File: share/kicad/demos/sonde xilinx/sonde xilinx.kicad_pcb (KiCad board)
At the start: 2 copper layers, 81.3 x 43.2 mm, 25 parts, among them J1 DB25MALE, J2 DB9MALE, P1 CONN_6, U1 74LS125, U2 74LS125

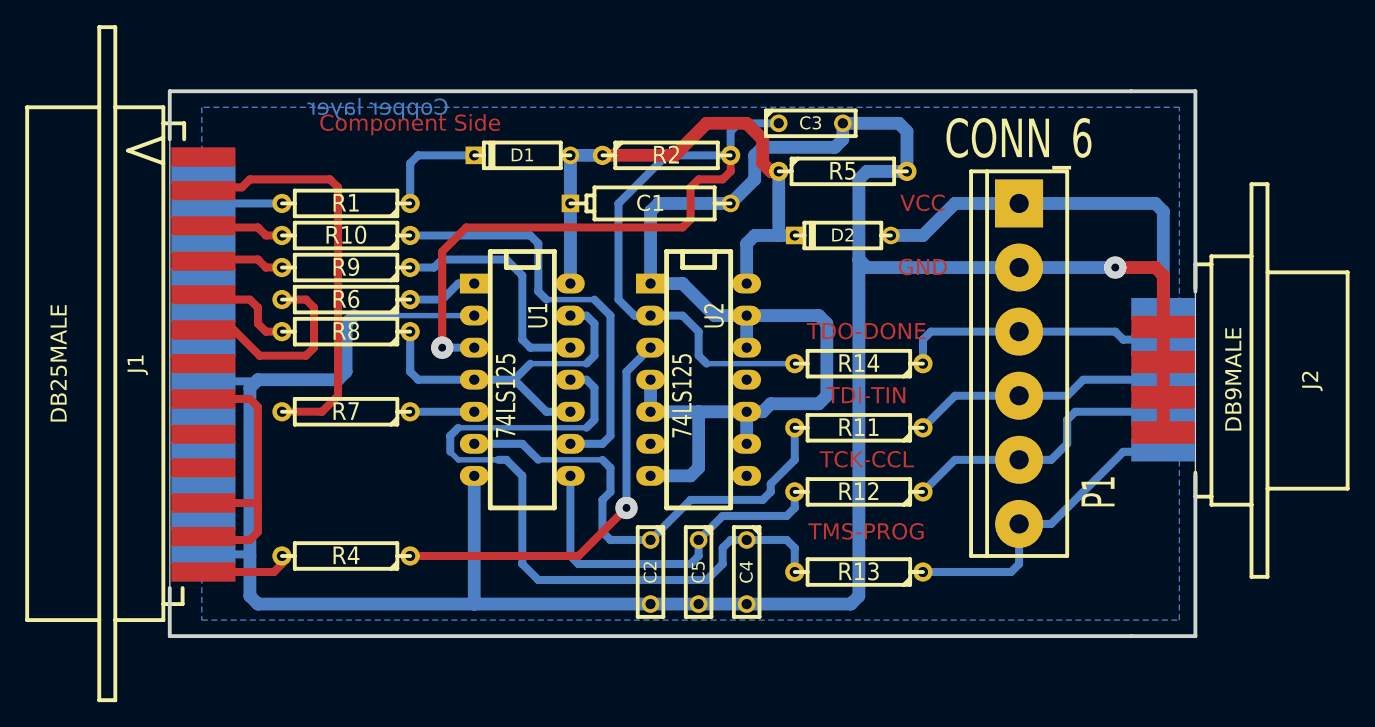
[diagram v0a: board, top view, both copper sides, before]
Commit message: Remove KiCad V4.0.7
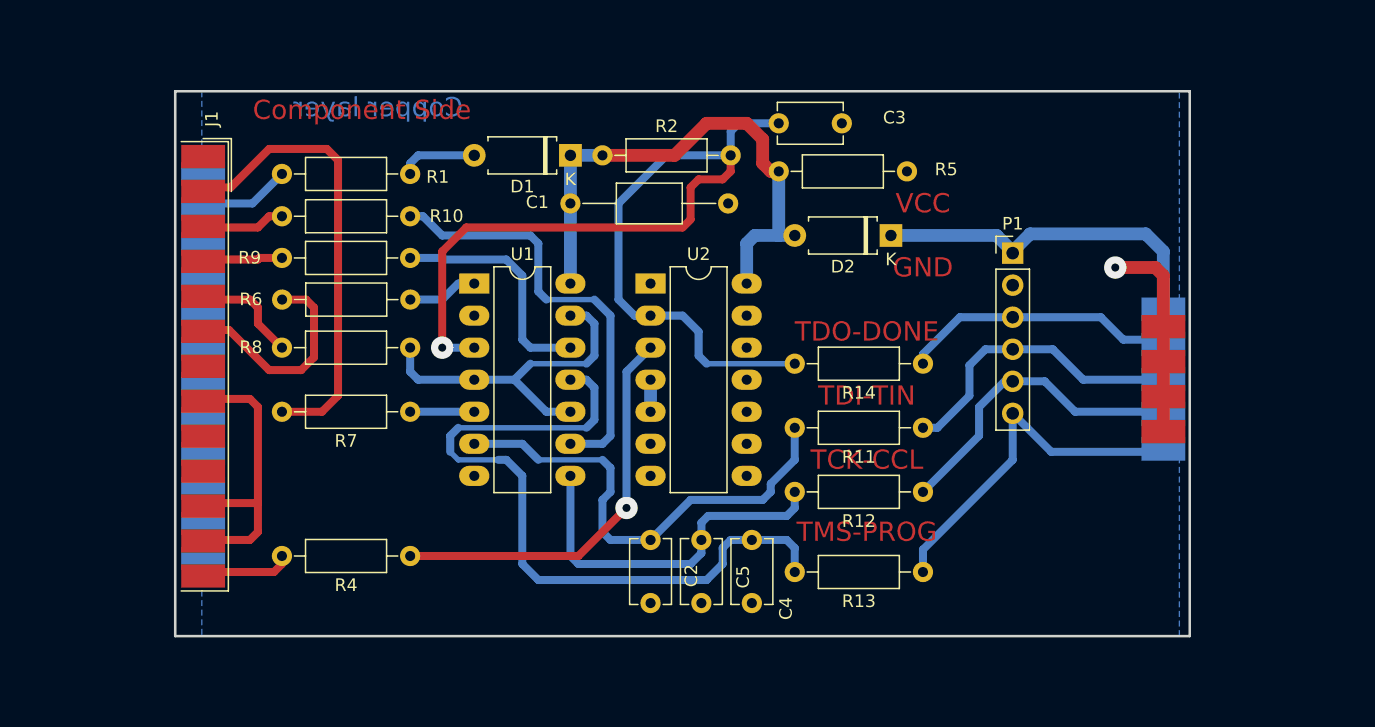
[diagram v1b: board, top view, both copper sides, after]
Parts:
- C1: footprint CP5 -> Capacitor_THT:C_Axial_L5.1mm_D3.1mm_P12.50mm_Horizontal
- C2, C3, C4, C5: footprint C2 -> Capacitor_THT:C_Disc_D5.1mm_W3.2mm_P5.00mm
- D1, D2: footprint D3 -> Diode_THT:D_A-405_P7.62mm_Horizontal
- J1: footprint DB25M_CI -> Connector_Dsub:DSUB-25_Male_EdgeMount_P2.77mm
- J2: footprint DB9M_CI_INVERT -> Connector_Dsub:DSUB-9_Male_EdgeMount_P2.77mm; moved to B.Cu
- P1: footprint bornier6 -> Connector_PinHeader_2.54mm:PinHeader_1x06_P2.54mm_Vertical
- R1, R10, R11, R12, R13, R14, R2, R4, R5, R6, R7, R8, R9: footprint R4 -> Resistor_THT:R_Axial_DIN0207_L6.3mm_D2.5mm_P10.16mm_Horizontal
- U1, U2: footprint 14DIP-ELL300 -> Package_DIP:DIP-14_W7.62mm_LongPads
- moved P1 8.78 mm to (169.7, 80.1), turned to 0 degrees
- moved U1 8.52 mm to (127.0, 82.5), turned to 0 degrees
- moved U2 8.52 mm to (141.0, 82.5), turned to 0 degrees
- moved C1 6.35 mm to (134.6, 76.2)
- moved R1 5.59 mm to (121.9, 73.9)
- moved R10 5.30 mm to (121.9, 77.2)
- moved R8 5.24 mm to (121.9, 87.6)
- moved R9 5.14 mm to (121.9, 80.5)
- moved R6 5.09 mm to (121.9, 83.8)
- moved R11 5.08 mm to (162.6, 94.0)
- moved R12 5.08 mm to (162.6, 99.1)
- moved R13 5.08 mm to (162.6, 105.4)
- moved R14 5.08 mm to (162.6, 88.9)
- moved R2 5.08 mm to (137.2, 72.4)
- moved R5 5.08 mm to (151.1, 73.7)
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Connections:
- J1 pad 1: (no net) -> unconnected-(J1-Pad1)
- J1 pad 10: (no net) -> unconnected-(J1-Pad10)
- J1 pad 14: (no net) -> unconnected-(J1-Pad14)
- J1 pad 16: (no net) -> unconnected-(J1-Pad16)
- J1 pad 17: (no net) -> unconnected-(J1-Pad17)
- J1 pad 18: (no net) -> unconnected-(J1-Pad18)
- J1 pad 19: (no net) -> unconnected-(J1-Pad19)
- J1 pad 21: (no net) -> unconnected-(J1-Pad21)
- J1 pad 22: (no net) -> unconnected-(J1-Pad22)
- J1 pad 23: (no net) -> unconnected-(J1-Pad23)
- J1 pad 24: (no net) -> unconnected-(J1-Pad24)
- J1 pad 7: (no net) -> unconnected-(J1-Pad7)
- J1 pad 9: (no net) -> unconnected-(J1-Pad9)
- U2 pad 11: (no net) -> unconnected-(U2-Pad11)
- U2 pad 6: (no net) -> unconnected-(U2-Pad6)
- U2 pad 8: (no net) -> unconnected-(U2-Pad8)
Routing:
- net GND: track 266.1 -> 19.1 mm
- net /TMS-PROG: track 25.0 -> 28.8 mm
- net /TDI-DIN: track 20.6 -> 24.0 mm
- net /TDI-DIN-D0: track 33.4 -> 36.7 mm
- net /PWR_3,3-5V: track 30.7 -> 27.9 mm
- net Net-(D1-Pad2): track 8.52 -> 6.18 mm
- net /TCK-CCLK: track 23.1 -> 25.3 mm
- net /TD0-PROG-D4: track 15.8 -> 17.2 mm
- net Net-(R8-Pad1): track 29.0 -> 27.8 mm
- net /VCC_SENSE-ERROR*: track 6.35 -> 7.32 mm
- net Net-(C5-Pad1): track 28.2 -> 28.9 mm
- net Net-(J1-Pad11): track 24.2 -> 23.5 mm
- net Net-(R10-Pad1): track 33.7 -> 34.3 mm
- net /CTRL-D3: track 8.55 -> 9.07 mm
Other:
- board size 81.3 x 43.2 mm -> 80.4 x 43.2 mm
- net class Default removed
- rule pad_to_mask_clearance: 0.254 -> 0
